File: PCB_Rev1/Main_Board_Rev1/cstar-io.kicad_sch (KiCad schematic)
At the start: 11 parts, among them J2 Conn_01x04_Socket, J3 691137710002, Q1 AO3400A, Q2 AO3400A, Q3 AO3400A, Q4 IRFHM9331TRPBF

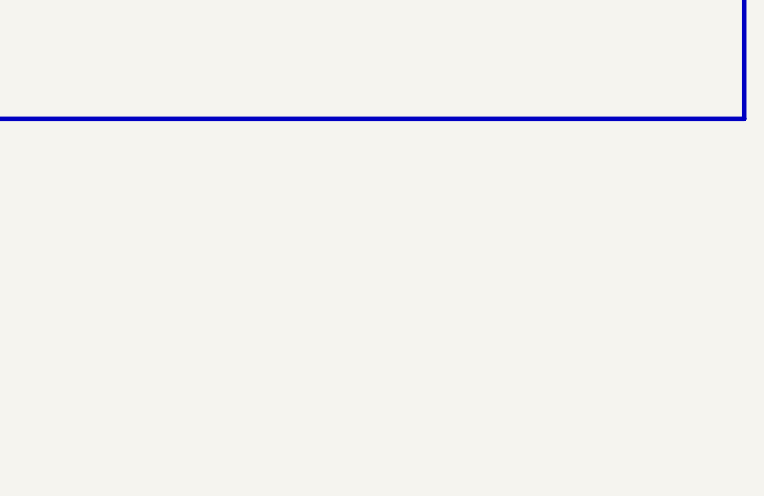
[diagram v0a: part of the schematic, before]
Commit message: Power nets updated in all schematics
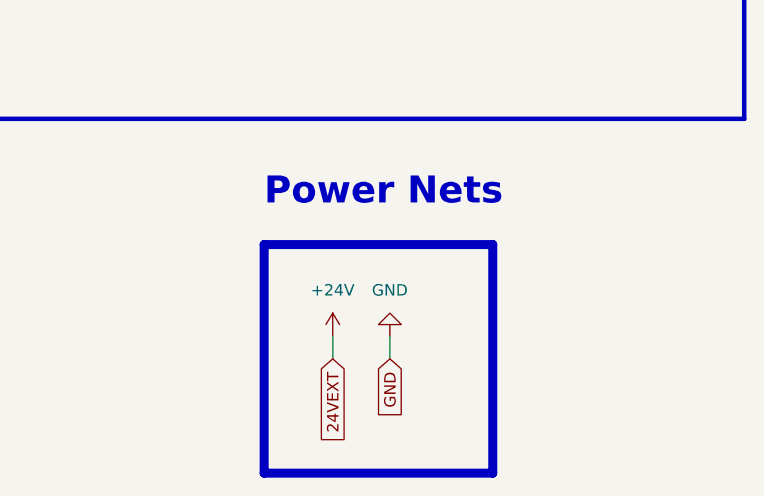
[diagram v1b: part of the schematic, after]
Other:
- note added: "Power Nets"
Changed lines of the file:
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@@
+	(wire
+		(pts
+			(xy 219.71 146.05) (xy 219.71 148.59)
+		)
+		(stroke
+			(width 0)
+			(type default)
+		)
+	)
 	(wire
 		(pts
@@
 	(wire
 		(pts
+			(xy 226.06 146.05) (xy 226.06 148.59)
+		)
+		(stroke
+			(width 0)
+			(type default)
+		)
+	)
+	(wire
+		(pts
 			(xy 92.71 56.515) (xy 125.73 56.515)
 		)
@@
 			(width 0)
 			(type default)
+		)
+	)
+	(rectangle
+		(start 212.09 135.89)
+		(end 237.49 161.29)
+		(stroke
+			(width 1)
+			(type default)
+		)
+		(fill
+			(type none)
 		)
 	)
@@
 		)
 	)
+	(text "Power Nets"
+		(exclude_from_sim no)
+		(at 212.09 131.826 0)
+		(effects
+			(font
+				(size 3 3)
+				(thickness 0.6)
+				(bold yes)
+			)
+			(justify left bottom)
+		)
+	)
 	(global_label "BATT_IN"
 		(shape input)
@@
 		)
 	)
+	(global_label "24VEXT"
+		(shape input)
+		(at 219.71 148.59 270)
+		(fields_autoplaced yes)
+		(effects
+			(font
+				(size 1.27 1.27)
+			)
+			(justify right)
+		)
+		(property "Intersheetrefs" "${INTERSHEET_REFS}"
+			(at 219.71 158.4089 90)
+			(effects
+				(font
+					(size 1.27 1.27)
+				)
+				(justify right)
+				(hide yes)
+			)
+		)
+	)
+	(global_label "GND"
+		(shape input)
+		(at 226.06 148.59 270)
+		(fields_autoplaced yes)
+		(effects
+			(font
+				(size 1.27 1.27)
+			)
+			(justify right)
+		)
+		(property "Intersheetrefs" "${INTERSHEET_REFS}"
+			(at 226.06 155.4457 90)
+			(effects
+				(font
+					(size 1.27 1.27)
+				)
+				(justify right)
+				(hide yes)
+			)
+		)
+	)
 	(global_label "RGB_Green_Control"
 		(shape input)
@@
 	)
 	(symbol
+		(lib_id "power:+5V")
+		(at 219.71 146.05 0)
+		(unit 1)
+		(exclude_from_sim no)
+		(in_bom yes)
+		(on_board yes)
+		(dnp no)
+		(fields_autoplaced yes)
+		(property "Reference" "#PWR053"
+			(at 219.71 149.86 0)
+			(effects
+				(font
+					(size 1.27 1.27)
+				)
+				(hide yes)
+			)
+		)
+		(property "Value" "+24V"
+			(at 219.71 140.97 0)
+			(effects
+				(font
+					(size 1.27 1.27)
+				)
+			)
+		)
+		(property "Footprint" ""
+			(at 219.71 146.05 0)
+			(effects
+				(font
+					(size 1.27 1.27)
+				)
+				(hide yes)
+			)
+		)
+		(property "Datasheet" ""
+			(at 219.71 146.05 0)
+			(effects
+				(font
+					(size 1.27 1.27)
+				)
+				(hide yes)
+			)
+		)
+		(property "Description" "Power symbol creates a global label with name \"+5V\""
+			(at 219.71 146.05 0)
+			(effects
+				(font
+					(size 1.27 1.27)
+				)
+				(hide yes)
+			)
+		)
+		(pin "1"
+		)
+		(instances
+			(project "Main_Board_Rev1"
+				(path "/8f5a23de-a1fa-4202-92fb-c2ac3de0338c/9a9c2aab-15db-457a-a1a3-5bc6a825b752"
+					(reference "#PWR053")
+					(unit 1)
+				)
+			)
+		)
+	)
+	(symbol
 		(lib_id "power:GND")
 		(at 214.63 85.725 0)
@@
 					(unit 1)
 				)
+			)
+		)
+	)
+	(symbol
+		(lib_id "power:GND")
+		(at 226.06 146.05 180)
+		(unit 1)
+		(exclude_from_sim no)
+		(in_bom yes)
+		(on_board yes)
+		(dnp no)
+		(fields_autoplaced yes)
+		(property "Reference" "#PWR061"
+			(at 226.06 139.7 0)
+			(effects
+				(font
+					(size 1.27 1.27)
+				)
+				(hide yes)
+			)
+		)
+		(property "Value" "GND"
+			(at 226.06 140.97 0)
+			(effects
+				(font
+					(size 1.27 1.27)
+				)
+			)
+		)
+		(property "Footprint" ""
+			(at 226.06 146.05 0)
+			(effects
+				(font
+					(size 1.27 1.27)
+				)
+				(hide yes)
+			)
+		)
+		(property "Datasheet" ""
+			(at 226.06 146.05 0)
+			(effects
+				(font
+					(size 1.27 1.27)
+				)
+				(hide yes)
+			)
+		)
+		(property "Description" "Power symbol creates a global label with name \"GND\" , ground"
+			(at 226.06 146.05 0)
+			(effects
+				(font
+					(size 1.27 1.27)
+				)
+				(hide yes)
+			)
+		)
+		(pin "1"
+		)
+		(instances
+			(project "Main_Board_Rev1"
+				(path "/8f5a23de-a1fa-4202-92fb-c2ac3de0338c/9a9c2aab-15db-457a-a1a3-5bc6a825b752"
+					(reference "#PWR061")
+					(unit 1)
+				)

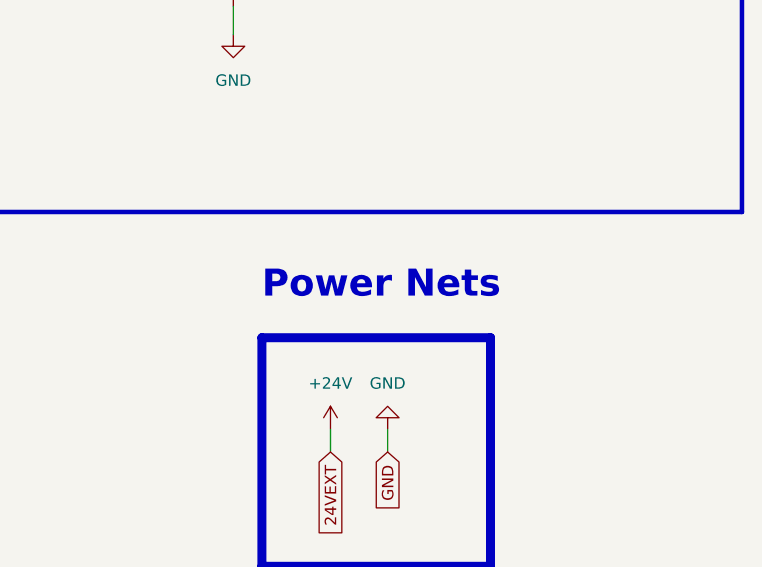
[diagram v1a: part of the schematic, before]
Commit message: Connections to RPi GPIO Pins + Eliminating Errors from Layout
Global net connections made from RPi GPIO pins.
Error for mounting hole corrected -> mounting hole symbol imported into schematic and correct footprint assigned.
Warnings for J10, J11, J12 connectors resolved- imported footprint for the connector from online (error in the one imported from KiCAD libraries with pins S1 and S2 labeled as MP in the footprint)
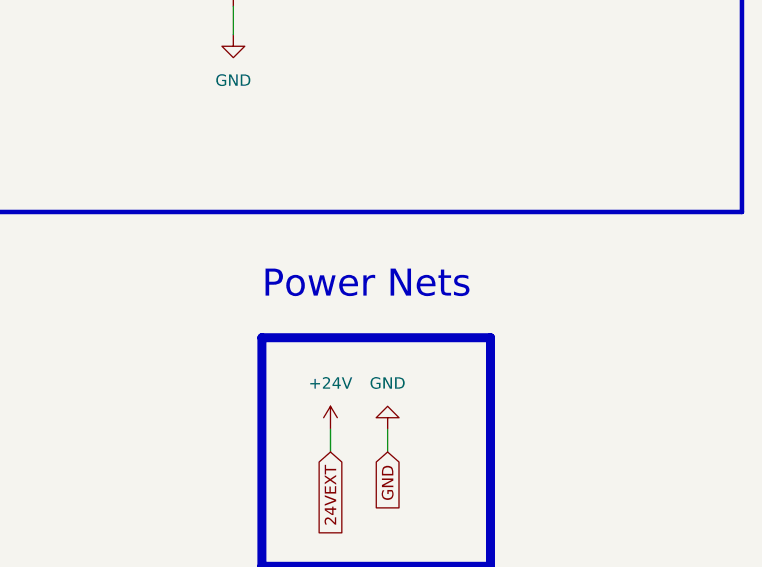
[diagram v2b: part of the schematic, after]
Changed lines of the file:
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@@
 			(font
 				(size 3 3)
-				(thickness 0.6)
-				(bold yes)
+				(thickness 0.375)
 			)
 			(justify left bottom)

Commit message: fixed soldering bridge issue
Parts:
- Q4: footprint Footprints:Power_FET -> Footprints:NEW_power_FET
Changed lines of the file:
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@@
 			)
 		)
-		(property "Footprint" "Footprints:Power_FET"
+		(property "Footprint" "Footprints:NEW_power_FET"
 			(at 219.075 63.5 0)
 			(effects

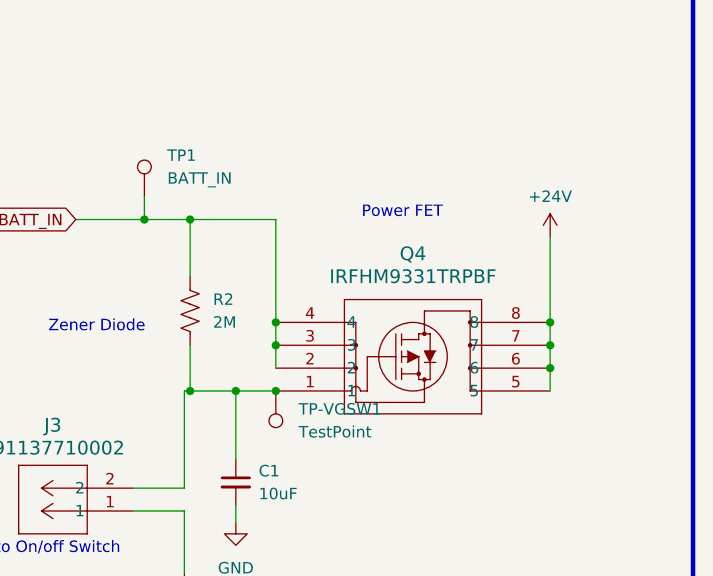
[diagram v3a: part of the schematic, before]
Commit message: Updated Footprint + Symbol for FET
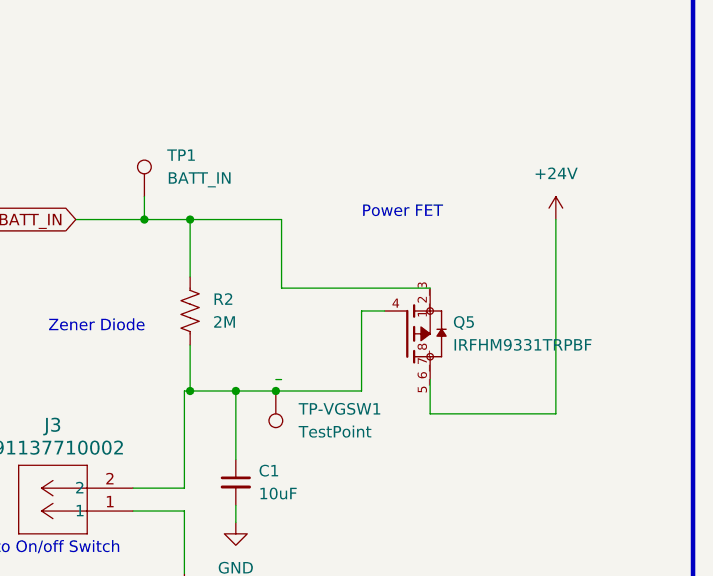
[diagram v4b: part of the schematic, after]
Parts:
- removed Q4: IRFHM9331TRPBF, Footprints:NEW_power_FET, symbol IRFHM9331TRPBF:IRFHM9331TRPBF
- added Q5: IRFHM9331TRPBF, Footprints:TRANS_IRFHM9331TRPBF, symbol PowerFET:IRFHM9331TRPBF
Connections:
- net +24V: now also Q5.5_6_7_8
- net BATT_IN: now also Q5.1_2_3
- net at C1.1, J3.2, R2.2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: now also Q5.4

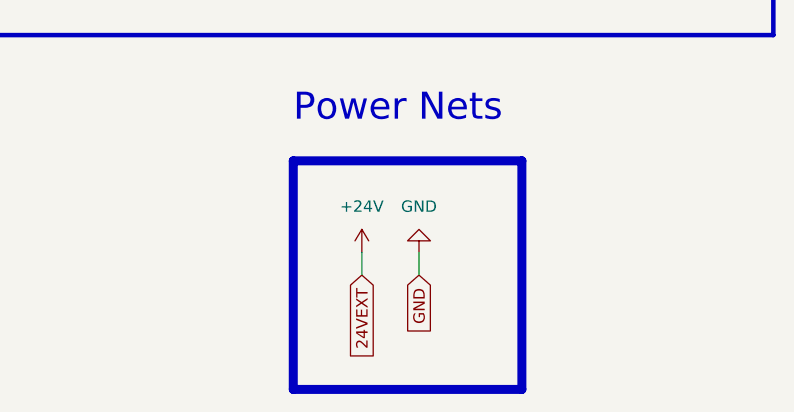
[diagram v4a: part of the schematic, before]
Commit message: 12V traces widths increased 1.016
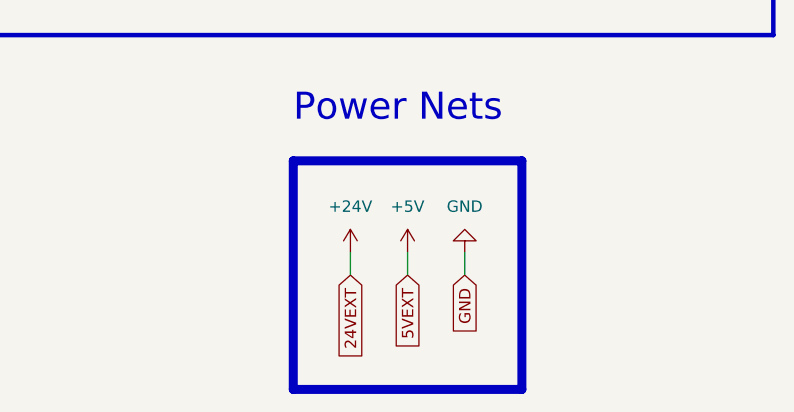
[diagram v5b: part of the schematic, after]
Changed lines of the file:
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@@
 	(wire
 		(pts
-			(xy 219.71 146.05) (xy 219.71 148.59)
+			(xy 218.44 146.05) (xy 218.44 148.59)
 		)
 		(stroke
@@
 	(wire
 		(pts
-			(xy 226.06 146.05) (xy 226.06 148.59)
+			(xy 231.14 146.05) (xy 231.14 148.59)
 		)
 		(stroke
@@
 		(pts
 			(xy 214.63 71.12) (xy 214.63 78.74)
+		)
+		(stroke
+			(width 0)
+			(type default)
+		)
+	)
+	(wire
+		(pts
+			(xy 224.79 146.05) (xy 224.79 148.59)
 		)
 		(stroke
@@
 		)
 	)
+	(global_label "5VEXT"
+		(shape input)
+		(at 224.79 148.59 270)
+		(fields_autoplaced yes)
+		(effects
+			(font
+				(size 1.27 1.27)
+			)
+			(justify right)
+		)
+		(property "Intersheetrefs" "${INTERSHEET_REFS}"
+			(at 224.79 157.1994 90)
+			(effects
+				(font
+					(size 1.27 1.27)
+				)
+				(justify right)
+				(hide yes)
+			)
+		)
+	)
 	(global_label "RGB_Blue_Control"
 		(shape input)
@@
 	(global_label "24VEXT"
 		(shape input)
-		(at 219.71 148.59 270)
+		(at 218.44 148.59 270)
 		(fields_autoplaced yes)
 		(effects
@@
 		)
 		(property "Intersheetrefs" "${INTERSHEET_REFS}"
-			(at 219.71 158.4089 90)
+			(at 218.44 158.4089 90)
 			(effects
 				(font
@@
 	(global_label "GND"
 		(shape input)
-		(at 226.06 148.59 270)
+		(at 231.14 148.59 270)
 		(fields_autoplaced yes)
 		(effects
@@
 		)
 		(property "Intersheetrefs" "${INTERSHEET_REFS}"
-			(at 226.06 155.4457 90)
+			(at 231.14 155.4457 90)
 			(effects
 				(font
@@
 	)
 	(symbol
+		(lib_id "power:+5V")
+		(at 224.79 146.05 0)
+		(unit 1)
+		(exclude_from_sim no)
+		(in_bom yes)
+		(on_board yes)
+		(dnp no)
+		(fields_autoplaced yes)
+		(property "Reference" "#PWR073"
+			(at 224.79 149.86 0)
+			(effects
+				(font
+					(size 1.27 1.27)
+				)
+				(hide yes)
+			)
+		)
+		(property "Value" "+5V"
+			(at 224.79 140.97 0)
+			(effects
+				(font
+					(size 1.27 1.27)
+				)
+			)
+		)
+		(property "Footprint" ""
+			(at 224.79 146.05 0)
+			(effects
+				(font
+					(size 1.27 1.27)
+				)
+				(hide yes)
+			)
+		)
+		(property "Datasheet" ""
+			(at 224.79 146.05 0)
+			(effects
+				(font
+					(size 1.27 1.27)
+				)
+				(hide yes)
+			)
+		)
+		(property "Description" "Power symbol creates a global label with name \"+5V\""
+			(at 224.79 146.05 0)
+			(effects
+				(font
+					(size 1.27 1.27)
+				)
+				(hide yes)
+			)
+		)
+		(pin "1"
+		)
+		(instances
+			(project "Main_Board_Rev1"
+				(path "/8f5a23de-a1fa-4202-92fb-c2ac3de0338c/9a9c2aab-15db-457a-a1a3-5bc6a825b752"
+					(reference "#PWR073")
+					(unit 1)
+				)
+			)
+		)
+	)
+	(symbol
 		(lib_id "Transistor_FET:AO3400A")
 		(at 64.77 64.77 0)
@@
 	(symbol
 		(lib_id "power:+5V")
-		(at 219.71 146.05 0)
+		(at 218.44 146.05 0)
 		(unit 1)
 		(exclude_from_sim no)
@@
 		(fields_autoplaced yes)
 		(property "Reference" "#PWR053"
-			(at 219.71 149.86 0)
+			(at 218.44 149.86 0)
 			(effects
 				(font
@@
 		)
 		(property "Value" "+24V"
-			(at 219.71 140.97 0)
+			(at 218.44 140.97 0)
 			(effects
 				(font
@@
 		)
 		(property "Footprint" ""
-			(at 219.71 146.05 0)
+			(at 218.44 146.05 0)
 			(effects
 				(font
@@
 		)
 		(property "Datasheet" ""
-			(at 219.71 146.05 0)
+			(at 218.44 146.05 0)
 			(effects
 				(font
@@
 		)
 		(property "Description" "Power symbol creates a global label with name \"+5V\""
-			(at 219.71 146.05 0)
+			(at 218.44 146.05 0)
 			(effects
 				(font
@@
 	(symbol
 		(lib_id "power:GND")
-		(at 226.06 146.05 180)
+		(at 231.14 146.05 180)
 		(unit 1)
 		(exclude_from_sim no)
@@
 		(fields_autoplaced yes)
 		(property "Reference" "#PWR061"
-			(at 226.06 139.7 0)
+			(at 231.14 139.7 0)
 			(effects
 				(font
@@
 		)
 		(property "Value" "GND"
-			(at 226.06 140.97 0)
+			(at 231.14 140.97 0)
 			(effects
 				(font
@@
 		)
 		(property "Footprint" ""
-			(at 226.06 146.05 0)
+			(at 231.14 146.05 0)
 			(effects
 				(font
@@
 		)
 		(property "Datasheet" ""
-			(at 226.06 146.05 0)
+			(at 231.14 146.05 0)
 			(effects
 				(font
@@
 		)
 		(property "Description" "Power symbol creates a global label with name \"GND\" , ground"
-			(at 226.06 146.05 0)
-			(effects
-				(font
+			(at 231.14 146.05 0)
+			(effects
+				(font

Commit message: LCSC + CSV changes
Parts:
- C1: LCSC (none) -> C2190942
- J2: LCSC (none) -> C566011
- J3: LCSC (none) -> C3819953
- Q1, Q2, Q3: LCSC (none) -> C20917
- Q5: LCSC (none) -> C148156
- R1, R2: LCSC (none) -> C114532
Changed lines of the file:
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@@
+			)
+		)
+		(property "LCSC" "C20917"
+			(at 64.77 64.77 0)
+			(effects
+				(font
+					(size 1.27 1.27)
+				)
+				(hide yes)
 			)
 		)
@@
 			)
 		)
+		(property "LCSC" "C148156"
+			(at 233.68 64.77 0)
+			(effects
+				(font
+					(size 1.27 1.27)
+				)
+				(hide yes)
+			)
+		)
 		(pin "1_2_3"
 		)
@@
 			)
 		)
+		(property "LCSC" "C114532"
+			(at 208.915 95.25 0)
+			(effects
+				(font
+					(size 1.27 1.27)
+				)
+				(hide yes)
+			)
+		)
 		(pin "1"
 		)
@@
 			)
 		)
+		(property "LCSC" "C20917"
+			(at 114.3 102.235 0)
+			(effects
+				(font
+					(size 1.27 1.27)
+				)
+				(hide yes)
+			)
+		)
 		(pin "1"
 		)
@@
 			)
 		)
+		(property "LCSC" "C3819953"
+			(at 203.2 84.455 0)
+			(effects
+				(font
+					(size 1.27 1.27)
+				)
+				(hide yes)
+			)
+		)
 		(pin "1"
 		)
@@
 			)
 		)
+		(property "LCSC" "C20917"
+			(at 90.17 85.725 0)
+			(effects
+				(font
+					(size 1.27 1.27)
+				)
+				(hide yes)
+			)
+		)
 		(pin "1"
 		)
@@
 			)
 		)
+		(property "LCSC" "C2190942"
+			(at 214.63 81.28 0)
+			(effects
+				(font
+					(size 1.27 1.27)
+				)
+				(hide yes)
+			)
+		)
 		(pin "1"
 		)
@@
 			)
 		)
+		(property "LCSC" "C114532"
+			(at 209.55 62.23 0)
+			(effects
+				(font
+					(size 1.27 1.27)
+				)
+				(hide yes)
+			)
+		)
 		(pin "1"
 		)
@@
 			(at 130.81 53.975 0)
 			(effects
+				(font
+					(size 1.27 1.27)
+				)
+				(hide yes)
+			)
+		)
+		(property "LCSC" "C566011"
+			(at 130.81 53.975 0)
+			(effects
